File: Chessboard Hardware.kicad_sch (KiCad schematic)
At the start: 20 parts, among them J1 Conn_01x04_Pin

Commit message: Finish placing except test points, which have 2.54 pin header footprint now
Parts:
- TP1, TP10, TP11, TP12, TP13, TP14, TP2, TP3, TP4, TP5, TP6, TP7, TP8, TP9: footprint TestPoint:TestPoint_THTPad_2.5x2.5mm_Drill1.2mm -> Connector_PinHeader_2.54mm:PinHeader_1x01_P2.54mm_Vertical
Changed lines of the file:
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@@
 			)
 		)
-		(property "Footprint" "TestPoint:TestPoint_THTPad_2.5x2.5mm_Drill1.2mm"
+		(property "Footprint" "Connector_PinHeader_2.54mm:PinHeader_1x01_P2.54mm_Vertical"
 			(at 196.85 93.98 0)
 			(effects
@@
 			)
 		)
-		(property "Footprint" "TestPoint:TestPoint_THTPad_2.5x2.5mm_Drill1.2mm"
+		(property "Footprint" "Connector_PinHeader_2.54mm:PinHeader_1x01_P2.54mm_Vertical"
 			(at 196.85 88.9 0)
 			(effects
@@
 			)
 		)
-		(property "Footprint" "TestPoint:TestPoint_THTPad_2.5x2.5mm_Drill1.2mm"
+		(property "Footprint" "Connector_PinHeader_2.54mm:PinHeader_1x01_P2.54mm_Vertical"
 			(at 199.39 25.4 0)
 			(effects
@@
 			)
 		)
-		(property "Footprint" "TestPoint:TestPoint_THTPad_2.5x2.5mm_Drill1.2mm"
+		(property "Footprint" "Connector_PinHeader_2.54mm:PinHeader_1x01_P2.54mm_Vertical"
 			(at 196.85 48.26 0)
 			(effects
@@
 			)
 		)
-		(property "Footprint" "TestPoint:TestPoint_THTPad_2.5x2.5mm_Drill1.2mm"
+		(property "Footprint" "Connector_PinHeader_2.54mm:PinHeader_1x01_P2.54mm_Vertical"
 			(at 196.85 43.18 0)
 			(effects
@@
 			)
 		)
-		(property "Footprint" "TestPoint:TestPoint_THTPad_2.5x2.5mm_Drill1.2mm"
+		(property "Footprint" "Connector_PinHeader_2.54mm:PinHeader_1x01_P2.54mm_Vertical"
 			(at 214.63 25.4 0)
 			(effects
@@
 			)
 		)
-		(property "Footprint" "TestPoint:TestPoint_THTPad_2.5x2.5mm_Drill1.2mm"
+		(property "Footprint" "Connector_PinHeader_2.54mm:PinHeader_1x01_P2.54mm_Vertical"
 			(at 196.85 104.14 0)
 			(effects
@@
 			)
 		)
-		(property "Footprint" "TestPoint:TestPoint_THTPad_2.5x2.5mm_Drill1.2mm"
+		(property "Footprint" "Connector_PinHeader_2.54mm:PinHeader_1x01_P2.54mm_Vertical"
 			(at 196.85 53.34 0)
 			(effects
@@
 			)
 		)
-		(property "Footprint" "TestPoint:TestPoint_THTPad_2.5x2.5mm_Drill1.2mm"
+		(property "Footprint" "Connector_PinHeader_2.54mm:PinHeader_1x01_P2.54mm_Vertical"
 			(at 196.85 58.42 0)
 			(effects
@@
 			)
 		)
-		(property "Footprint" "TestPoint:TestPoint_THTPad_2.5x2.5mm_Drill1.2mm"
+		(property "Footprint" "Connector_PinHeader_2.54mm:PinHeader_1x01_P2.54mm_Vertical"
 			(at 196.85 73.66 0)
 			(effects
@@
 			)
 		)
-		(property "Footprint" "TestPoint:TestPoint_THTPad_2.5x2.5mm_Drill1.2mm"
+		(property "Footprint" "Connector_PinHeader_2.54mm:PinHeader_1x01_P2.54mm_Vertical"
 			(at 196.85 83.82 0)
 			(effects
@@
 			)
 		)
-		(property "Footprint" "TestPoint:TestPoint_THTPad_2.5x2.5mm_Drill1.2mm"
+		(property "Footprint" "Connector_PinHeader_2.54mm:PinHeader_1x01_P2.54mm_Vertical"
 			(at 196.85 78.74 0)
 			(effects
@@
 			)
 		)
-		(property "Footprint" "TestPoint:TestPoint_THTPad_2.5x2.5mm_Drill1.2mm"
+		(property "Footprint" "Connector_PinHeader_2.54mm:PinHeader_1x01_P2.54mm_Vertical"
 			(at 196.85 99.06 0)
 			(effects
@@
 			)
 		)
-		(property "Footprint" "TestPoint:TestPoint_THTPad_2.5x2.5mm_Drill1.2mm"
+		(property "Footprint" "Connector_PinHeader_2.54mm:PinHeader_1x01_P2.54mm_Vertical"
 			(at 196.85 68.58 0)
 			(effects

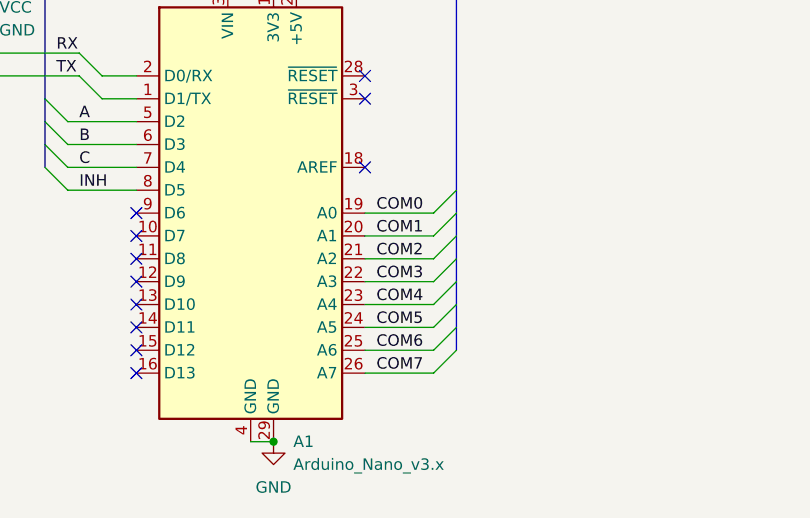
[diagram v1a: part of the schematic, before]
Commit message: Done routing everything except linear halls
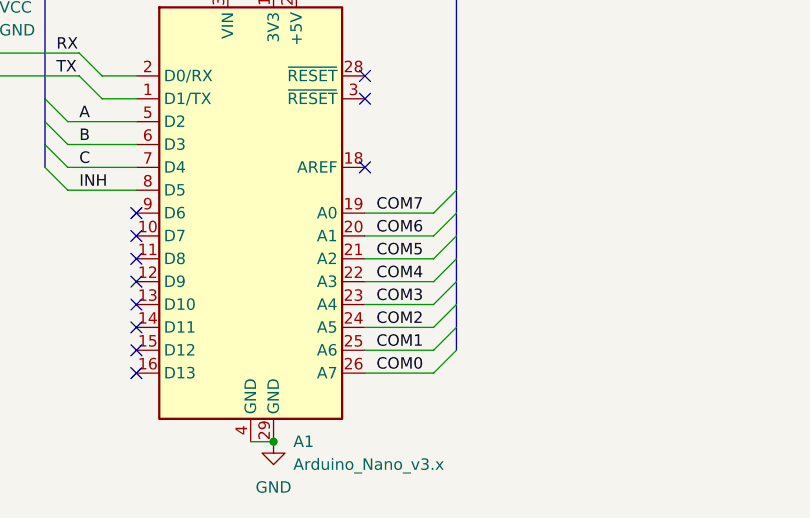
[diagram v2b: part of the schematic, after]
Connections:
- net COM0: now also A1.26 (A7); no longer A1.19 (A0)
- net COM1: now also A1.25 (A6); no longer A1.20 (A1)
- net COM2: now also A1.24 (A5); no longer A1.21 (A2)
- net COM3: now also A1.23 (A4); no longer A1.22 (A3)
- net COM4: now also A1.22 (A3); no longer A1.23 (A4)
- net COM5: now also A1.21 (A2); no longer A1.24 (A5)
- net COM6: now also A1.20 (A1); no longer A1.25 (A6)
- net COM7: now also A1.19 (A0); no longer A1.26 (A7)
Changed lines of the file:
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@@
 	)
 	(label "COM0"
-		(at 78.74 158.75 0)
+		(at 78.74 176.53 0)
 		(effects
 			(font
@@
 	)
 	(label "COM7"
-		(at 78.74 176.53 0)
+		(at 78.74 158.75 0)
 		(effects
 			(font
@@
 	)
 	(label "COM4"
+		(at 78.74 166.37 0)
+		(effects
+			(font
+				(size 1.27 1.27)
+			)
+			(justify left bottom)
+		)
+	)
+	(label "B"
+		(at 45.72 107.95 0)
+		(effects
+			(font
+				(size 1.27 1.27)
+			)
+			(justify left bottom)
+		)
+	)
+	(label "COM3"
 		(at 78.74 168.91 0)
-		(effects
-			(font
-				(size 1.27 1.27)
-			)
-			(justify left bottom)
-		)
-	)
-	(label "B"
-		(at 45.72 107.95 0)
-		(effects
-			(font
-				(size 1.27 1.27)
-			)
-			(justify left bottom)
-		)
-	)
-	(label "COM3"
-		(at 78.74 166.37 0)
 		(effects
 			(font
@@
 	)
 	(label "COM6"
-		(at 78.74 173.99 0)
+		(at 78.74 161.29 0)
 		(effects
 			(font
@@
 	)
 	(label "COM5"
-		(at 78.74 171.45 0)
+		(at 78.74 163.83 0)
 		(effects
 			(font
@@
 	)
 	(label "COM2"
-		(at 78.74 163.83 0)
+		(at 78.74 171.45 0)
 		(effects
 			(font
@@
 	)
 	(label "COM1"
-		(at 78.74 161.29 0)
-		(effects
-			(font
+		(at 78.74 173.99 0)
+		(effects
+			(font

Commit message: Add Arduino Nano model
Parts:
- A1: footprint Module:Arduino_Nano -> Project Library:Arduino_Nano
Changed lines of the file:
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@@
 			)
 		)
-		(property "Footprint" "Module:Arduino_Nano"
+		(property "Footprint" "Project Library:Arduino_Nano"
 			(at 64.77 158.75 0)
 			(effects

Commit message: JST XH connector
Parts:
- J1: footprint Connector_PinHeader_2.54mm:PinHeader_1x04_P2.54mm_Vertical -> Connector_JST:JST_XH_B4B-XH-A_1x04_P2.50mm_Vertical
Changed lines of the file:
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@@
 			)
 		)
-		(property "Footprint" "Connector_PinHeader_2.54mm:PinHeader_1x04_P2.54mm_Vertical"
+		(property "Footprint" "Connector_JST:JST_XH_B4B-XH-A_1x04_P2.50mm_Vertical"
 			(at 27.94 138.43 0)
 			(effects
